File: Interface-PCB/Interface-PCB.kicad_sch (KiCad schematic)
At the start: 14 parts, among them J1 BARREL_JACK_PAD, J2 BARREL_JACK_PAD, J3 GPIO_DEBUG_HEADER, J4 RASPBERRYPI_GPIO_CONN_HEADER, J5 I2C_HEADER, M1 PERISTALTIC_PUMP, M2 PERISTALTIC_PUMP, M3 PERISTALTIC_PUMP, U1 TB6612FNG_BREAKOUT, U2 TB6612FNG_BREAKOUT

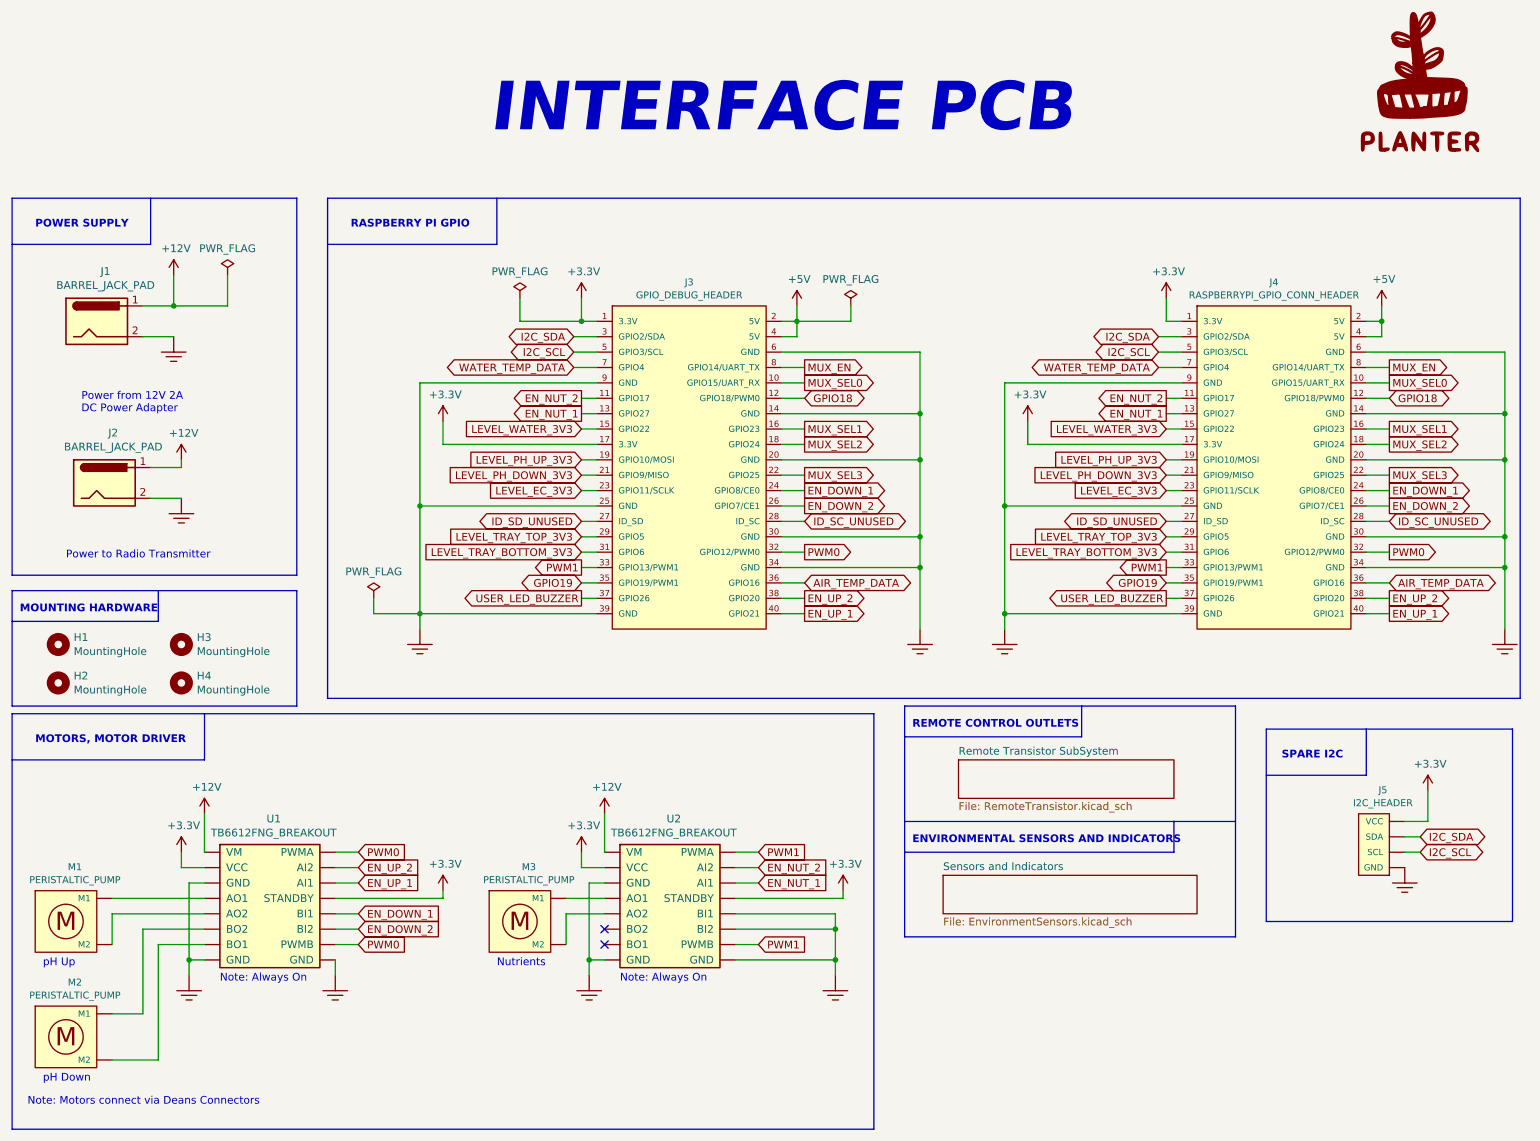
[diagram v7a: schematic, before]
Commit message: Complete Initial Layout of PCB
- aligned to 5mm grid
- 100x100mm board
- update footprints
- align 2 resistors to 2.54mm spacing
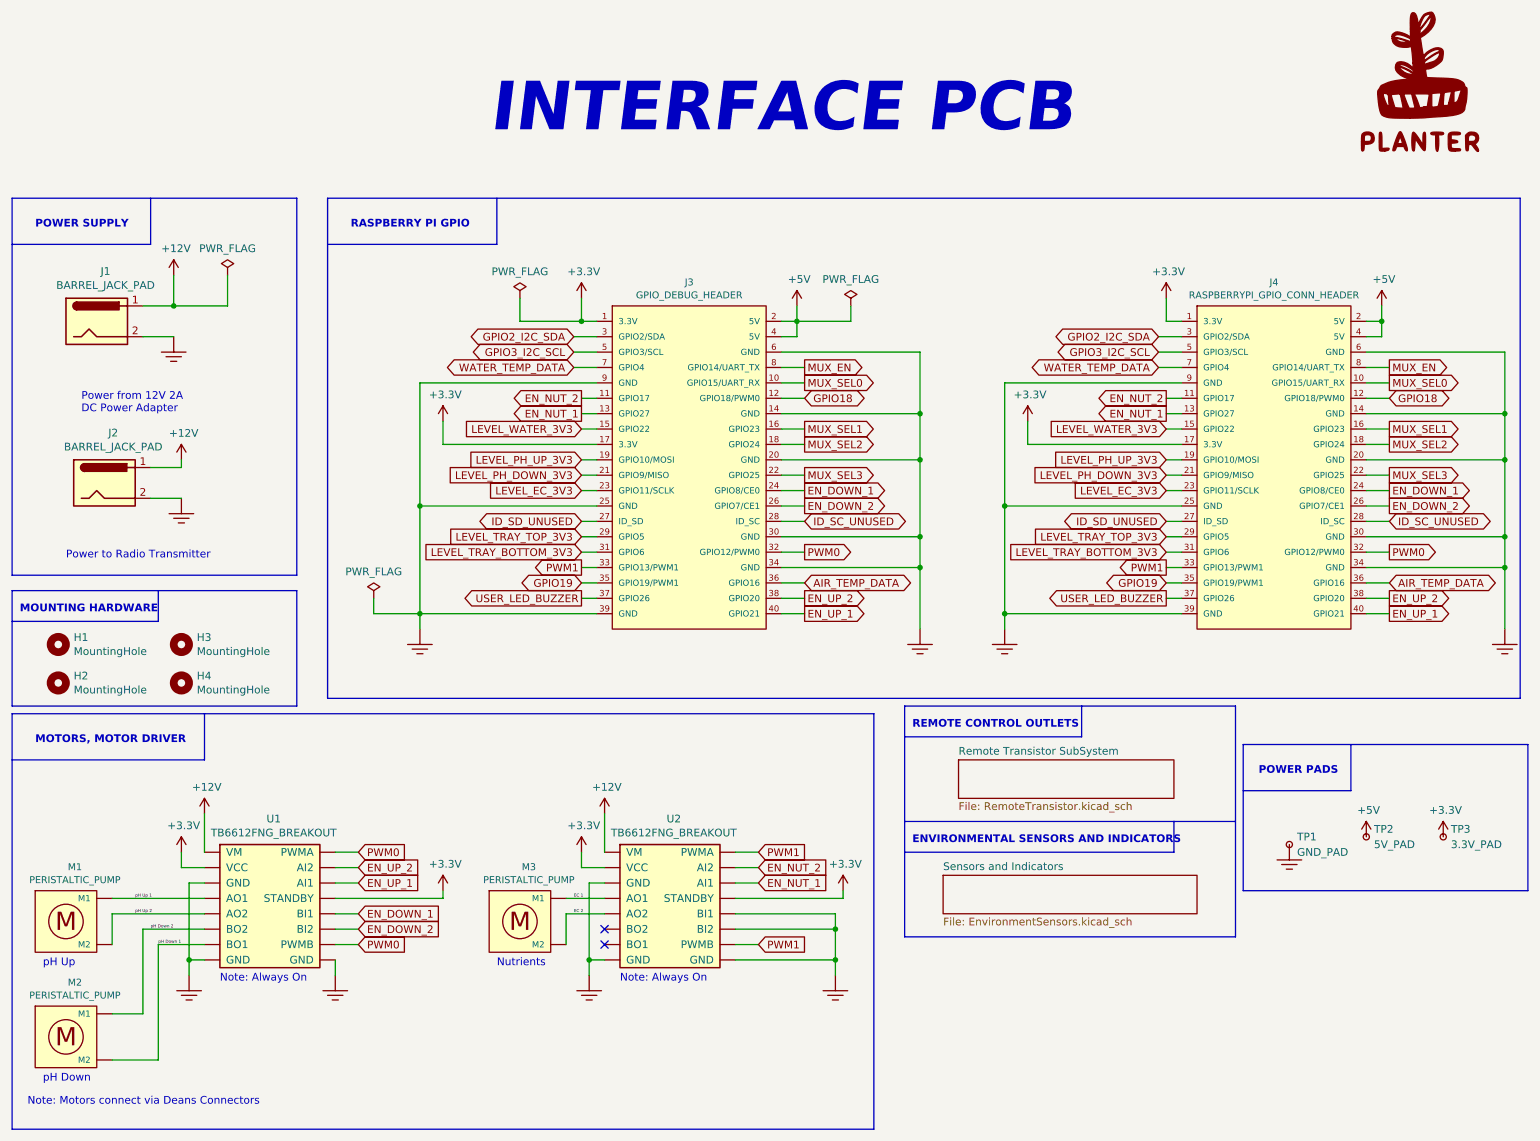
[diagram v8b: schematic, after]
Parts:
- removed J5: I2C_HEADER, AA_Custom_Components:JST_XH_1x04_P2.54mm_Vertical, symbol AA_Custom_Components:I2C_HEADER
- added TP1: GND_PAD, AA_Custom_Components:TestPoint_Pad_4.0x4.0mm, symbol Connector:TestPoint_Small
- added TP2: 5V_PAD, AA_Custom_Components:TestPoint_Pad_4.0x4.0mm, symbol Connector:TestPoint_Small
- added TP3: 3.3V_PAD, AA_Custom_Components:TestPoint_Pad_4.0x4.0mm, symbol Connector:TestPoint_Small
- J1, J2, M1, M2, M3: footprint AA_Custom_Components:PowerPad_Pair_5.0x5.0mm -> AA_Custom_Components:PowerPad_Pair_4.0x4.0mm
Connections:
- net +3V3: now also TP3.1
- net +5V: now also TP2.1
- net GND: now also TP1.1
- net pH Up 1: now reaches M1.1 (M1), U1.4 (AO1)
- net pH Up 2: now reaches M1.2 (M2), U1.5 (AO2)
- net pH Down 2: now reaches M2.1 (M1), U1.6 (BO2)
- net pH Down 1: now reaches M2.2 (M2), U1.7 (BO1)
- net EC 1: now reaches M3.1 (M1), U2.4 (AO1)
- net EC 2: now reaches M3.2 (M2), U2.5 (AO2)
- net I2C_SCL renamed GPIO3_I2C_SCL
- net I2C_SDA renamed GPIO2_I2C_SDA
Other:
- note added: "POWER PADS"
- note removed: "SPARE I2C"
